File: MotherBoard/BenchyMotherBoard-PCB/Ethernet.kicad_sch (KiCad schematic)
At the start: 5 parts, among them J23 RJ45-CONN-TRANSFORMER, J24 RJ45-CONN-TRANSFORMER, U23 KSZ8081MNXIA-TR, U24 KSZ8081MNXIA-TR, U4 AM6254ATCGGAALW

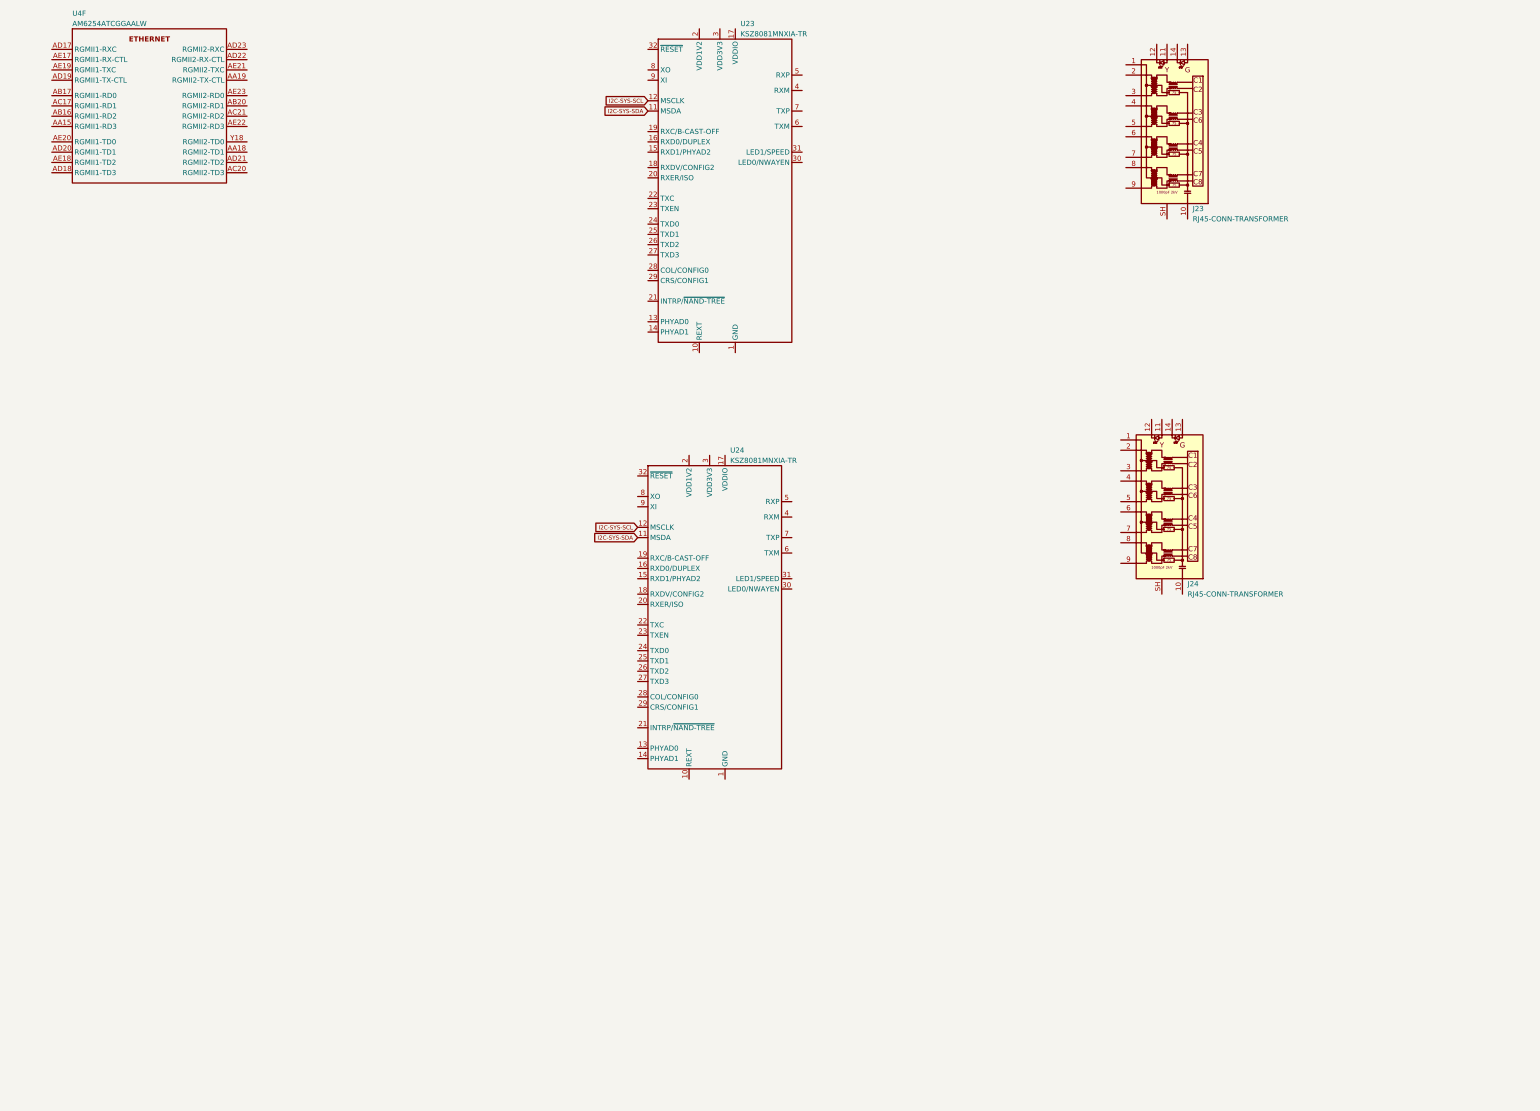
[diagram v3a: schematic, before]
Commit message: Add new ethernet chip - KSZ9031
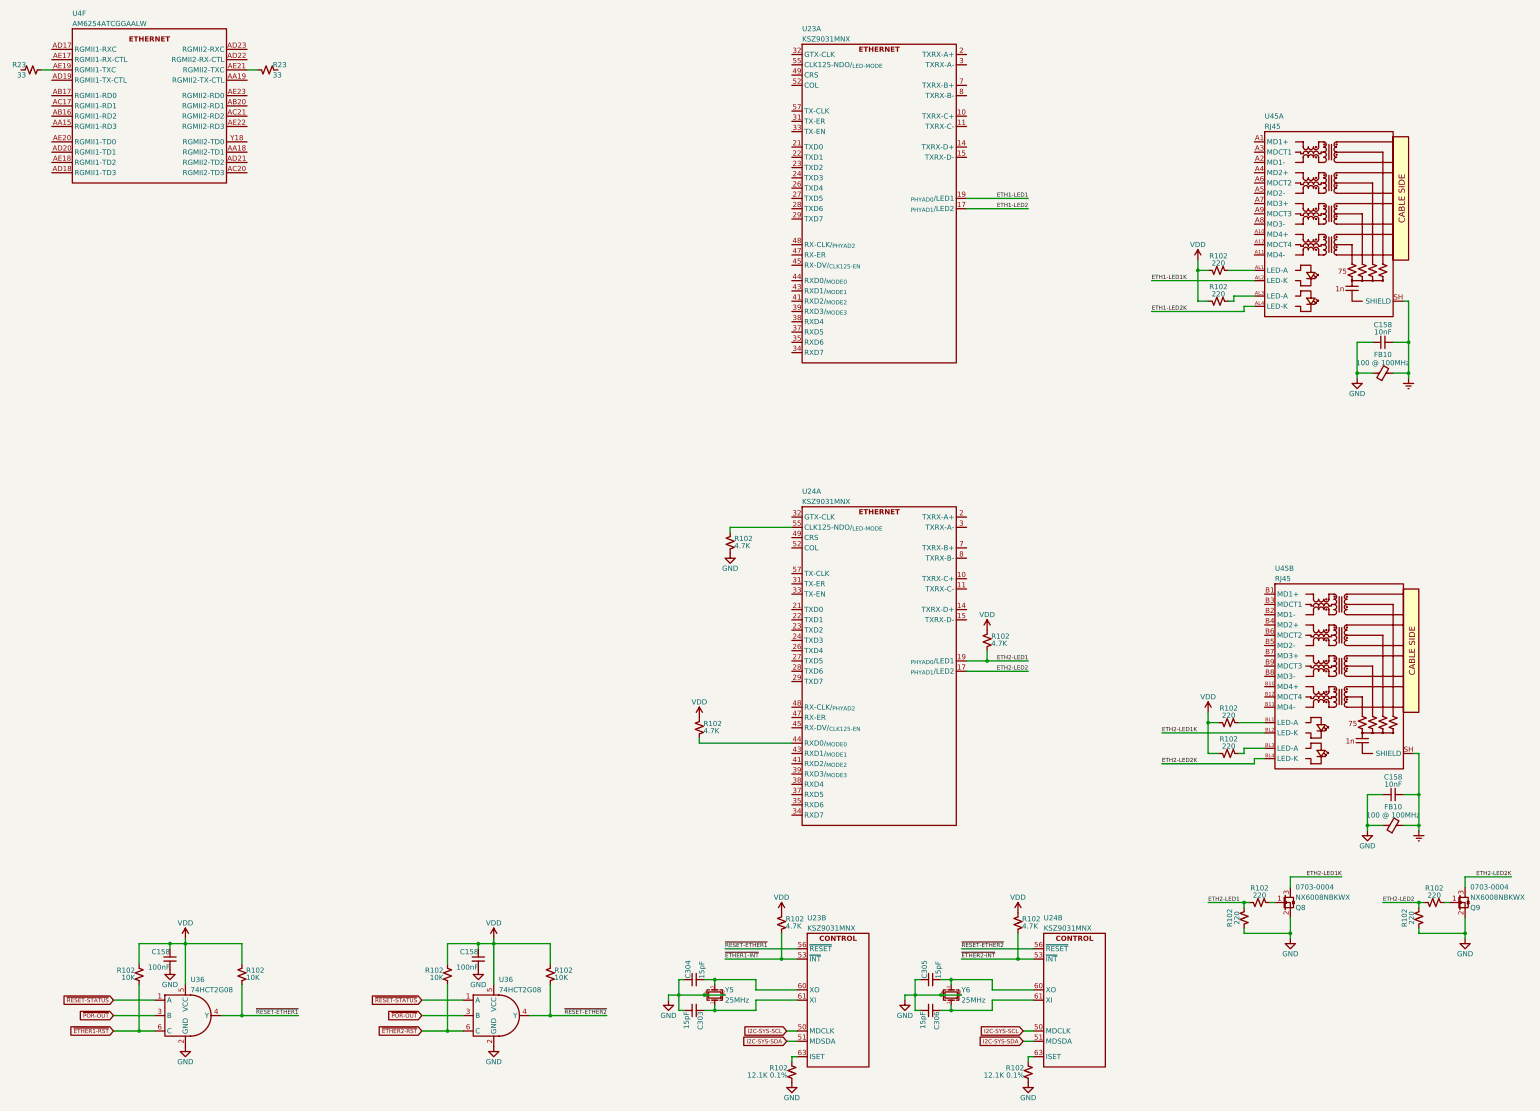
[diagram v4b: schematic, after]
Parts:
- removed J23, J24: RJ45-CONN-TRANSFORMER, Daxxn_Connectors:RJ45_Wuerth_7499111446_Horizontal, symbol Daxxn_Connectors:RJ45-CONN-TRANSFORMER
- removed U23, U24: KSZ8081MNXIA-TR, Package_DFN_QFN:QFN-32-1EP_5x5mm_P0.5mm_EP3.1x3.1mm, symbol Daxxn_IC:KSZ8081MNXIA-TR
- added C158 (x2): 10nF, Capacitor_SMD:C_0201_0603Metric, symbol Daxxn_Device:C
- added C158 (x2): 100nF, Capacitor_SMD:C_0201_0603Metric, symbol Daxxn_Device:C
- added C303, C304, C305, C306: 15pF, Capacitor_SMD:C_0201_0603Metric, symbol Daxxn_Device:C
- added FB10 (x2): 100 @ 100MHz, Inductor_SMD:L_0603_1608Metric, symbol Daxxn_Device:FerriteBead
- added Q8, Q9: NX6008NBKWX, Package_TO_SOT_SMD:SOT-323_SC-70, symbol Daxxn_Transistors:NX6008NBKWX
- added R102 (x4): 10K, Resistor_SMD:R_0402_1005Metric, symbol Daxxn_Device:R
- added R102 (x5): 4.7K, Resistor_SMD:R_0402_1005Metric, symbol Daxxn_Device:R
- added R102 (x8): 220, Resistor_SMD:R_0402_1005Metric, symbol Daxxn_Device:R
- added R102 (x2): 12.1K 0.1%, Resistor_SMD:R_0402_1005Metric, symbol Daxxn_Device:R
- added R23 (x2): 33, Resistor_SMD:R_0201_0603Metric, symbol Daxxn_Device:R
- added U23, U24: KSZ9031MNX, Daxxn_Packages:QFN-64-1EP_8x8mm_P0.4mm_EP6.5x6.5mm, symbol Daxxn_IC:KSZ9031MNX
- added U36 (x2): 74HCT2G08, Daxxn_Packages:WSON-6_1.5x1.5mm_P0.5mm, symbol Daxxn_Logic:SN74LVC1G11DRYR
- added U45: RJ45, symbol Daxxn_Connectors:RJ45-DUAL-TRANS-VD
- added Y5, Y6: 25MHz, symbol Daxxn_Device:Crystal
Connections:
- net GND: now also C158.1, C158.1, C158.2, C158.2, C303.2, C304.1, C305.1, C306.2, FB10.1, FB10.1, Q8.2 (S), Q9.2 (S), R102.1, R102.1, R102.1, R102.2, R102.2, U36.2 (GND), U36.2 (GND), Y5.2, Y5.4, Y6.2, Y6.4
- net I2C-SYS-SCL: now also U23.50 (MDCLK), U24.50 (MDCLK)
- net I2C-SYS-SDA: now also U23.51 (MDSDA), U24.51 (MDSDA)
- net at U4.AE19 (RGMII1-TXC): now also R23.2
- net at U4.AE21 (RGMII2-TXC): now also R23.2
- new net: U23.6 (NC), U23.62 (NC)
- new net: C304.2, U23.60 (XO), Y5.3
- new net: C303.1, U23.61 (XI), Y5.1
- new net: R102.2, U23.63 (ISET)
- new net: R102.1, U45.BL1 (LED-A)
- new net: C306.1, U24.61 (XI), Y6.1
- new net: C305.2, U24.60 (XO), Y6.3
- new net: U24.6 (NC), U24.62 (NC)
- new net: R102.2, U24.63 (ISET)
- new net: R102.1, U45.AL3 (LED-A)
- new net: R102.1, U24.44 (RXD0/_{MODE0})
- new net: R102.2, U24.55 (CLK125-NDO/_{LED-MODE})
- new net: Q9.1 (G), R102.1
- new net: Q8.1 (G), R102.1
- new net: R102.1, U45.BL3 (LED-A)
- new net: R102.1, U45.AL1 (LED-A)
- new net ETH1-LED1: U23.19 (_{PHYAD0}/LED1)
- new net ETH1-LED1K: U45.AL2 (LED-K)
- new net ETH1-LED2: U23.17 (_{PHYAD1}/LED2)
- new net ETH1-LED2K: U45.AL4 (LED-K)
- new net ETH2-LED1: R102.1, R102.1, R102.2, U24.19 (_{PHYAD0}/LED1)
- new net ETH2-LED1K: Q8.3 (D), U45.BL2 (LED-K)
- new net ETH2-LED2: R102.1, R102.2, U24.17 (_{PHYAD1}/LED2)
- new net ETH2-LED2K: Q9.3 (D), U45.BL4 (LED-K)
- new net SHIELD: C158.2, C158.2, FB10.2, FB10.2, U45.SH (SHIELD), U45.SH (SHIELD)
- new net VDD: C158.1, C158.1, R102.2, R102.2, R102.2, R102.2, R102.2, R102.2, R102.2, R102.2, R102.2, R102.2, R102.2, R102.2, U36.5 (VCC), U36.5 (VCC)
- new net ~{ETHER1-INT}: R102.1, U23.53 (~{INT})
- new net ~{ETHER1-RST}: R102.1, U36.6 (C)
- new net ~{ETHER2-INT}: R102.1, U24.53 (~{INT})
- new net ~{ETHER2-RST}: R102.1, U36.6 (C)
- new net ~{POR-OUT}: U36.3 (B), U36.3 (B)
- new net ~{RESET-ETHER1}: R102.1, U23.56 (~{RESET}), U36.4 (Y)
- new net ~{RESET-ETHER2}: R102.1, U24.56 (~{RESET}), U36.4 (Y)
- new net ~{RESET-STATUS}: U36.1 (A), U36.1 (A)

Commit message: (WIP) Almost done with schematic
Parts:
- removed C303, C304, C305, C306: 15pF, Capacitor_SMD:C_0201_0603Metric, symbol Daxxn_Device:C
- removed Q8, Q9: NX6008NBKWX, Package_TO_SOT_SMD:SOT-323_SC-70, symbol Daxxn_Transistors:NX6008NBKWX
- removed R102 (x6): 220, Resistor_SMD:R_0402_1005Metric, symbol Daxxn_Device:R
- removed R102 (x3): 4.7K, Resistor_SMD:R_0402_1005Metric, symbol Daxxn_Device:R
- removed U23, U24: KSZ9031MNX, Daxxn_Packages:QFN-64-1EP_8x8mm_P0.4mm_EP6.5x6.5mm, symbol Daxxn_IC:KSZ9031MNX
- removed Y5, Y6: 25MHz, symbol Daxxn_Device:Crystal
- added C158 (x8): 100nF, Capacitor_SMD:C_0603_1608Metric, symbol Daxxn_Device:C
- added R102 (x4): 4.7K, Resistor_SMD:R_0201_0603Metric, symbol Daxxn_Device:R
- added R102 (x20): 10K, Resistor_SMD:R_0201_0603Metric, symbol Daxxn_Device:R
- added R102 (x2): 220, Resistor_SMD:R_0402_1005Metric, symbol Daxxn_Device:R
- added R23 (x2): 22, Resistor_SMD:R_0201_0603Metric, symbol Daxxn_Device:R
- added TP16: TP-ETH2-CLK, TestPoint:TestPoint_Pad_1.5x1.5mm, symbol Connector:TestPoint
- added TP17: TP-ETH1-CLK, TestPoint:TestPoint_Pad_1.5x1.5mm, symbol Connector:TestPoint
- added U23, U24: KSZ9021RN, Daxxn_Packages:QFN-48-1EP_7x7mm_P0.5mm_EP5.15x5.15mm, symbol Daxxn_IC:KSZ9021RN
- C158: footprint Capacitor_SMD:C_0201_0603Metric -> Capacitor_SMD:C_0603_1608Metric
- R102: footprint Resistor_SMD:R_0402_1005Metric -> Resistor_SMD:R_0201_0603Metric
- R102: value 12.1K 0.1% -> 4.99K 1%
- R23: value 33 -> 22
- U45: footprint (none) -> Daxxn_Connectors:RJMG212S21130ER
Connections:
- net ETH1-LED1: now also R102.1, R102.1, R102.2, U23.15 (LED2/_{PHYAD1})
- net ETH1-LED2: now also R102.1, R102.1, R102.2, U23.17 (LED1/_{PHYAD0})
- net ETH2-LED1: now also R102.1, R102.1, R102.2, U24.15 (LED2/_{PHYAD1})
- net ETH2-LED2: now also R102.1, R102.1, R102.2, U24.17 (LED1/_{PHYAD0})
- net GND: now also R102.1, R102.1, C158.1, C158.1, C158.1, C158.1, C158.1, C158.1, C158.1, C158.1, R102.1, R102.1, R102.1, R102.1, R102.1, R102.1, R102.1, R102.1, R102.1, R102.1, R102.1, R102.1, R102.1, R102.1
- net VDD: now also U45.AL1 (LED-A), U45.AL3 (LED-A), U45.BL1 (LED-A), U45.BL3 (LED-A), R102.1, R102.1, R102.2, R102.2, R102.2, R102.2, R102.2, R102.2, R102.2, R102.2; no longer R102.2, R102.2, R102.2, R102.2
- net ~{ETHER1-INT}: now also U23.38 (~{INT})
- net ~{ETHER2-INT}: now also U24.38 (~{INT})
- net ~{RESET-ETHER1}: now also R102.2, U23.42 (~{RESET}); no longer R102.1
- net ~{RESET-ETHER2}: now also R102.2, U24.42 (~{RESET}); no longer R102.1
- net at R102.2: now also U23.48 (ISET)
- net at R102.2: now also U24.48 (ISET)
- net ETH2-RX3: now reaches U4.AA15 (RGMII1-RD3)
- net ETH2-RX3: now also R102.2, U24.27 (RXD3/_{MODE3})
- net ETH1-TX1: now reaches U4.AA18 (RGMII2-TD1)
- net ETH1-TX1: now also U23.20 (TXD1)
- net ETH1-TX-EN: now reaches U4.AA19 (RGMII2-TX-CTL)
- net ETH1-TX-EN: now also U23.25 (TX-EN)
- net ETH2-RX2: now reaches U4.AB16 (RGMII1-RD2)
- net ETH2-RX2: now also R102.2, U24.28 (RXD2/_{MODE2})
- net ETH2-RX0: now reaches U4.AB17 (RGMII1-RD0)
- net ETH2-RX0: now also R102.2, U24.32 (RXD0/_{MODE0})
- net ETH1-RX1: now reaches U4.AB20 (RGMII2-RD1)
- net ETH1-RX1: now also R102.2, U23.31 (RXD1/_{MODE1})
- net ETH2-RX1: now reaches U4.AC17 (RGMII1-RD1)
- net ETH2-RX1: now also R102.2, U24.31 (RXD1/_{MODE1})
- net ETH1-TX3: now reaches U4.AC20 (RGMII2-TD3)
- net ETH1-TX3: now also U23.22 (TXD3)
- net ETH1-RX2: now reaches U4.AC21 (RGMII2-RD2)
- net ETH1-RX2: now also R102.2, U23.28 (RXD2/_{MODE2})
- net ETH2-RX-CLK: now reaches U4.AD17 (RGMII1-RXC)
- net ETH2-RX-CLK: now also R102.2, R23.1
- net ETH2-TX3: now reaches U4.AD18 (RGMII1-TD3)
- net ETH2-TX3: now also U24.22 (TXD3)
- net ETH2-TX-EN: now reaches U4.AD19 (RGMII1-TX-CTL)
- net ETH2-TX-EN: now also U24.25 (TX-EN)
- net ETH2-TX1: now reaches U4.AD20 (RGMII1-TD1)
- net ETH2-TX1: now also U24.20 (TXD1)
- net ETH1-TX2: now reaches U4.AD21 (RGMII2-TD2)
- net ETH1-TX2: now also U23.21 (TXD2)
- net ETH1-RX-DV: now reaches U4.AD22 (RGMII2-RX-CTL)
- net ETH1-RX-DV: now also R102.2, U23.33 (RX-DV/_{CLK125-EN})
- net ETH1-RX-CLK: now reaches U4.AD23 (RGMII2-RXC)
- net ETH1-RX-CLK: now also R102.2, R23.1
- net ETH2-RX-DV: now reaches U4.AE17 (RGMII1-RX-CTL)
- net ETH2-RX-DV: now also R102.2, U24.33 (RX-DV/_{CLK125-EN})
- net ETH2-TX2: now reaches U4.AE18 (RGMII1-TD2)
- net ETH2-TX2: now also U24.21 (TXD2)
- net ETH2-TX0: now reaches U4.AE20 (RGMII1-TD0)
- net ETH2-TX0: now also U24.19 (TXD0)
- net ETH1-RX3: now reaches U4.AE22 (RGMII2-RD3)
- net ETH1-RX3: now also R102.2, U23.27 (RXD3/_{MODE3})
- net ETH1-RX0: now reaches U4.AE23 (RGMII2-RD0)
- net ETH1-RX0: now also R102.2, U23.32 (RXD0/_{MODE0})
- net ETH1-TX0: now reaches U4.Y18 (RGMII2-TD0)
- net ETH1-TX0: now also U23.19 (TXD0)
- net ETH1-GTX-CLK: now reaches R23.1
- net ETH1-GTX-CLK: now also U23.24 (GTX-CLK)
- net ETH2-GTX-CLK: now reaches R23.1
- net ETH2-GTX-CLK: now also U24.24 (GTX-CLK)
- net ETH1-PHY-A+: now reaches U45.A1 (MD1+)
- net ETH1-PHY-A+: now also U23.2 (TXRX-A+)
- net ETH1-PHY-D+: now reaches U45.A10 (MD4+)
- net ETH1-PHY-D+: now also U23.10 (TXRX-D+)
- net ETH1-PHY-D-: now reaches U45.A11 (MD4-)
- net ETH1-PHY-D-: now also U23.11 (TXRX-D-)
- net at U45.A12 (MDCT4): now also C158.2
- net ETH1-PHY-A-: now reaches U45.A2 (MD1-)
- net ETH1-PHY-A-: now also U23.3 (TXRX-A-)
- net at U45.A3 (MDCT1): now also C158.2
- net ETH1-PHY-B+: now reaches U45.A4 (MD2+)
- net ETH1-PHY-B+: now also U23.5 (TXRX-B+)
- net ETH1-PHY-B-: now reaches U45.A5 (MD2-)
- net ETH1-PHY-B-: now also U23.6 (TXRX-B-)
- net at U45.A6 (MDCT2): now also C158.2
- net ETH1-PHY-C+: now reaches U45.A7 (MD3+)
- net ETH1-PHY-C+: now also U23.7 (TXRX-C+)
- net ETH1-PHY-C-: now reaches U45.A8 (MD3-)
- net ETH1-PHY-C-: now also U23.8 (TXRX-C-)
- net at U45.A9 (MDCT3): now also C158.2
- net ETH2-PHY-A+: now reaches U45.B1 (MD1+)
- net ETH2-PHY-A+: now also U24.2 (TXRX-A+)
- net ETH2-PHY-D+: now reaches U45.B10 (MD4+)
- net ETH2-PHY-D+: now also U24.10 (TXRX-D+)
- net ETH2-PHY-D-: now reaches U45.B11 (MD4-)
- net ETH2-PHY-D-: now also U24.11 (TXRX-D-)
- net at U45.B12 (MDCT4): now also C158.2
- net ETH2-PHY-A-: now reaches U45.B2 (MD1-)
- net ETH2-PHY-A-: now also U24.3 (TXRX-A-)
- net at U45.B3 (MDCT1): now also C158.2
- net ETH2-PHY-B+: now reaches U45.B4 (MD2+)
- net ETH2-PHY-B+: now also U24.5 (TXRX-B+)
- net ETH2-PHY-B-: now reaches U45.B5 (MD2-)
- net ETH2-PHY-B-: now also U24.6 (TXRX-B-)
- net at U45.B6 (MDCT2): now also C158.2
- net ETH2-PHY-C+: now reaches U45.B7 (MD3+)
- net ETH2-PHY-C+: now also U24.7 (TXRX-C+)
- net ETH2-PHY-C-: now reaches U45.B8 (MD3-)
- net ETH2-PHY-C-: now also U24.8 (TXRX-C-)
- net at U45.B9 (MDCT3): now also C158.2
- net ETH1-LED1K: no longer names the net of U45.AL2 (LED-K)
- net ETH1-LED1K: now also R102.2
- net ETH1-LED2K: no longer names the net of U45.AL4 (LED-K)
- net ETH1-LED2K: now also R102.2
- net ETH2-LED1K: no longer names the net of U45.BL2 (LED-K)
- net ETH2-LED1K: now also R102.2
- net ETH2-LED2K: no longer names the net of U45.BL4 (LED-K)
- net ETH2-LED2K: now also R102.2
- new net: TP17.1, U23.45 (XO)
- new net: R23.2, U24.35 (RX-CLK/_{PHYAD2})
- new net: TP16.1, U24.45 (XO)
- new net: R23.2, U23.35 (RX-CLK/_{PHYAD2})
- new net ETH1-CLKIN: U23.46 (XI)
- new net ETH1-LED-MODE: R102.1, U23.41 (CLK125-NDO/_{LED-MODE})
- new net ETH2-CLKIN: U24.46 (XI)
- new net ETH2-LED-MODE: R102.1, U24.41 (CLK125-NDO/_{LED-MODE})
- new net MDIO0-MDC: R102.1, U23.36 (MD-SCL), U24.36 (MD-SCL), U4.AD24 (MDIO0-MDC)
- new net MDIO0-MDIO: R102.1, U23.37 (MD-SDA), U24.37 (MD-SDA), U4.AB22 (MDIO0-MDIO)
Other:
- note added: "0"
- note added: "0001"
- note added: "011"
- note added: "1"
- note added: "111"
- note added: "125MHz CLOCK"
- note added: "3"
- note added: "7"
- note added: "CLK125-EN"
- note added: "DISABLE"
- note added: "ETHERNET CHANNEL 1"
- note added: "ETHERNET CHANNEL 2"
- note added: "GMII/MII"
- note added: "LED MODE"
- note added: "LED-MODE"
- note added: "MODE"
- note added: "MODE[3:0]"
- note added: "PHY ADDR"
- note added: "PHYAD[2:0]"
- note added: "PLACE NEAR PWR INPUT"
- note added: "SINGLE"
- note added: "STRAPPING OPTIONS"
- moved on the sheet: C158, FB10, R102, R23, U45A, U45B

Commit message: Start PCB layout
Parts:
- added R23 (x2): 0, Resistor_SMD:R_0201_0603Metric, symbol Daxxn_Device:R
- renumbered TP17 to TP16, TP16 to TP17, U24 to U13, U45 to U49, U23 to U9
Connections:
- net ETH1-RX-CLK: now also R23.2
- net ETH2-RX-CLK: now also R23.2
- new net RMII-REF-CLK: R23.1, R23.1

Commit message: (WIP) Still laying out PCB
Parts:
- removed FB10 (x2): 100 @ 100MHz, Inductor_SMD:L_0603_1608Metric, symbol Daxxn_Device:FerriteBead
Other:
- moved on the sheet: C158
